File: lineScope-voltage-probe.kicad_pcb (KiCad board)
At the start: 2 copper layers, 99.5 x 30 mm, 25 parts, among them J3 Conn_01x03, T1 TV19G

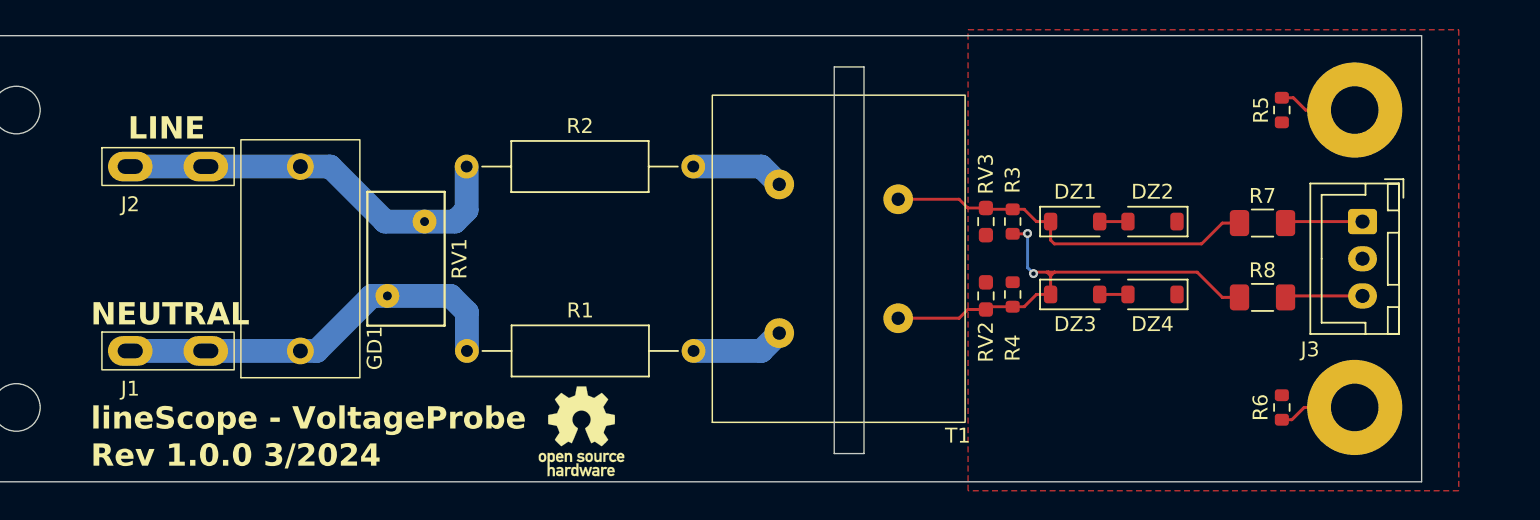
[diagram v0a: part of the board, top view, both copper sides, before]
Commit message: Add passtrought connector
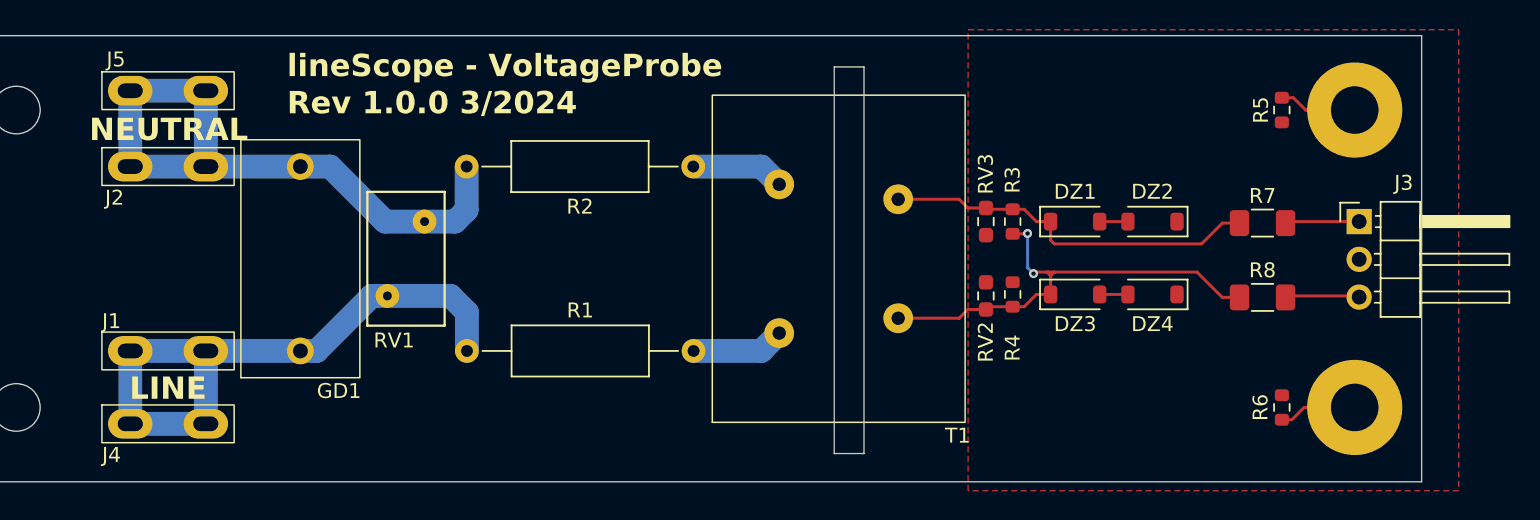
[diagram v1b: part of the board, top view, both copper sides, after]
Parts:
- removed REF**: OSHW-Logo_5.7x6mm_SilkScreen, Symbol:OSHW-Logo_5.7x6mm_SilkScreen
- added J4: ~, Koszalix_Connectors_Tab:TE-1-726388-2, F.Cu at (77.2, 120.5)
- added J5: ~, Koszalix_Connectors_Tab:TE-1-726388-2, F.Cu at (77.2, 98.1)
- J3: footprint Connector_JST:JST_XH_B3B-XH-A_1x03_P2.50mm_Vertical -> Connector_PinHeader_2.54mm:PinHeader_1x03_P2.54mm_Horizontal
- moved J3 0.22 mm to (157.3, 106.9), turned to 0 degrees
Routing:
- net /HV_{N}: track 27.4 -> 42.7 mm
- net /HV_{L}: track 27.2 -> 42.1 mm

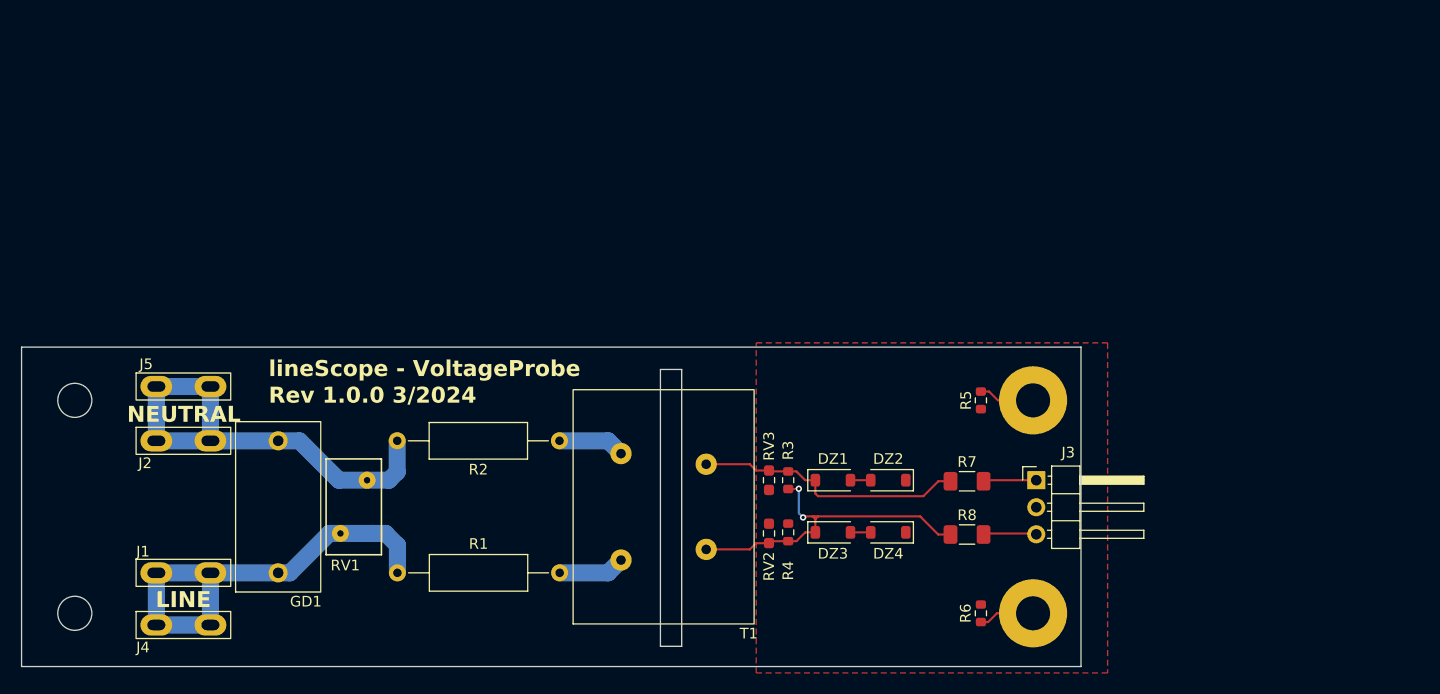
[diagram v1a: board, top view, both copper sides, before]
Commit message: Fill title block, add documentations
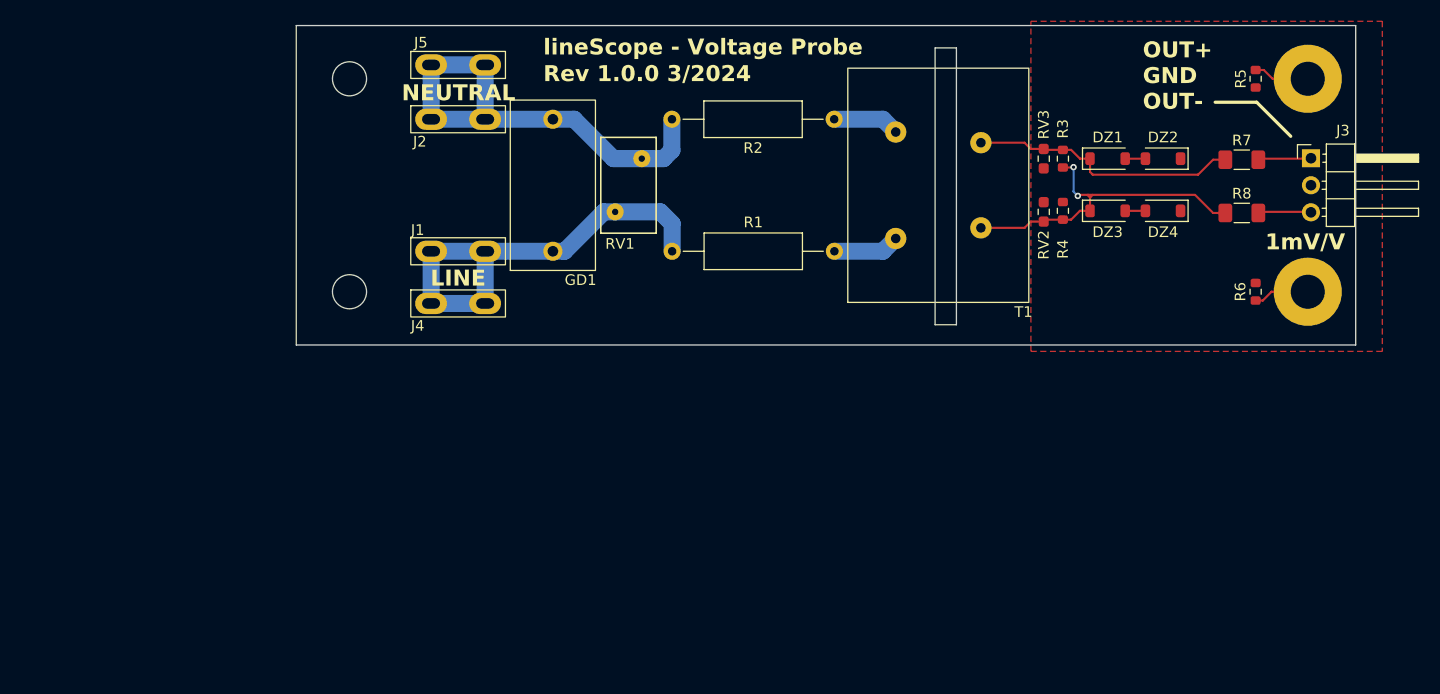
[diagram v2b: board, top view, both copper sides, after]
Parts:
- moved J3 39.8 mm to (183.1, 76.7)
- moved DZ1 39.7 mm to (164.0, 76.7)
- moved DZ3 39.7 mm to (164.0, 81.6)
- moved GD1 39.7 mm to (111.9, 79.2)
- moved H3 39.7 mm to (182.8, 69.2)
- moved H4 39.7 mm to (182.8, 89.2)
- moved R3 39.7 mm to (159.8, 76.7)
- moved R4 39.7 mm to (159.8, 81.6)
- moved R5 39.7 mm to (177.9, 69.2)
- moved R6 39.7 mm to (177.9, 89.2)
- moved RV2 39.7 mm to (158.0, 81.7)
- moved RV3 39.7 mm to (158.0, 76.7)
- moved H1 39.7 mm to (92.8, 69.2)
- moved H2 39.7 mm to (92.8, 89.2)
- moved J2 39.7 mm to (103.0, 73.0)
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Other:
- board text added: "0"
- board text added: "0 mm"
- board text added: "0,0000 mm / 0,0000 mm"
- board text added: "0,01 mm"
- board text added: "0,02"
- board text added: "0,035 mm"
- board text added: "0,3000 mm"
- board text added: "1"
- board text added: "1,51 mm"
- board text added: "1,6000 mm"
- board text added: "1mV/V"
- board text added: "2"
- board text added: "3,3"
- board text added: "4,5"
- board text added: "99,5000 mm x 30,0000 mm"
- board text added: "B.Cu"
- board text added: "B.Mask"
- board text added: "B.Paste"
- board text added: "B.Silkscreen"
- board text added: "BOARD CHARACTERISTICS"
- board text added: "Board Thickness:"
- board text added: "Board overall dimensions:"
- board text added: "Bottom Silk Screen"
- board text added: "Bottom Solder Mask"
- board text added: "Bottom Solder Paste"
- board text added: "Castellated pads:"
- board text added: "Color"
- board text added: "Copper Finish:"
- board text added: "Copper Layer Count:"
- board text added: "Dielectric 1"
- board text added: "Edge card connectors:"
- board text added: "Epsilon R"
- board text added: "F.Cu"
- board text added: "F.Mask"
- board text added: "F.Paste"
- board text added: "F.Silkscreen"
- board text added: "FR4"
- board text added: "HAL SnPb"
- board text added: "Impedance Control:"
- board text added: "Layer Name"
- board text added: "Loss Tangent"
- board text added: "Material"
- board text added: "Min hole diameter:"
- board text added: "Min track/spacing:"
- board text added: "No"
- board text added: "Not specified"
- board text added: "OUT+ GND OUT-"
- board text added: "Plated Board Edge:"
- board text added: "Thickness (mm)"
- board text added: "Top Silk Screen"
- board text added: "Top Solder Mask"
- board text added: "Top Solder Paste"
- board text added: "Type"
- board text added: "copper"
- board text added: "core"
- board text added: "lineScope - Voltage Probe"
- board text removed: "lineScope - VoltageProbe"

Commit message: Minor fixes
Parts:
- added REF1: Attention, Koszalix_Symbols:Attention, F.Cu at (98.0, 74.4)
- added REF2: OSHW-Logo2_7.3x6mm_SilkScreen, Symbol:OSHW-Logo2_7.3x6mm_SilkScreen, F.Cu at (112.5, 67.2)
- added REF3: WEEE-Logo_4.2x6mm_SilkScreen, Symbol:WEEE-Logo_4.2x6mm_SilkScreen, F.Cu at (173.6, 90.6)
- J3: value Conn_01x03 -> ~; footprint Connector_PinHeader_2.54mm:PinHeader_1x03_P2.54mm_Horizontal -> Koszalix_Connectors_Tab:TE-1-726388-2
- J5: value ~ -> Conn_01x03; footprint Koszalix_Connectors_Tab:TE-1-726388-2 -> Connector_PinHeader_2.54mm:PinHeader_1x03_P2.54mm_Horizontal
- moved J3 81.3 mm to (103.0, 90.4)
- moved J5 80.6 mm to (183.1, 76.7)
- moved J4 22.3 mm to (103.0, 68.0)
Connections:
- J3 pad 1: Net-(J3-Pin_1) -> /HV_{L}
- J4 pad 1: /HV_{L} -> /HV_{N}
- J5 pad 1: /HV_{N} -> Net-(J5-Pin_1)
- R7 pad 2: Net-(J3-Pin_1) -> Net-(J5-Pin_1)
- R8 pad 2: Net-(J3-Pin_3) -> Net-(J5-Pin_3)
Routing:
- net Net-(J5-Pin_1): track 0.00 -> 5.32 mm
- net Net-(J3-Pin_1): track 5.32 -> 0.00 mm
- net Net-(J5-Pin_3): track 0.00 -> 5.22 mm
- net Net-(J3-Pin_3): track 5.22 -> 0.00 mm
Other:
- board text added: "HIGH VOLTAGE"

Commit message: Fix TV19G
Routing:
- net Net-(DZ3-Pad1): track 31.7 -> 29.7 mm
- net /HV_{N'}: track 6.28 -> 4.28 mm
- net /HV_{L'}: track 6.26 -> 4.26 mm
- net Net-(DZ1-Pad1): track 25.5 -> 23.5 mm
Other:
- board text added: "Dielectric"
- board text removed: "Dielectric 1"
